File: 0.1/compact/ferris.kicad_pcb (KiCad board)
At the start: 2 copper layers, 208.7 x 86.7 mm, 102 parts, among them J1 USB C, K0_0 KEYSW, K0_1 KEYSW, K0_2 KEYSW, K0_3 KEYSW, K0_4 KEYSW, K0_5 KEYSW, K0_6 KEYSW, K0_7 KEYSW, K0_8 KEYSW, K0_9 KEYSW, K1_0 KEYSW, K1_1 KEYSW, K1_2 KEYSW, K1_3 KEYSW, K1_4 KEYSW, K1_5 KEYSW, K1_6 KEYSW, K1_7 KEYSW, K1_8 KEYSW, K1_9 KEYSW, K2_0 KEYSW, K2_1 KEYSW, K2_2 KEYSW, K2_3 KEYSW, K2_4 KEYSW, K2_5 KEYSW, K2_6 KEYSW, K2_7 KEYSW, K2_8 KEYSW, K2_9 KEYSW, K3_3 KEYSW, K3_4 KEYSW, K3_5 KEYSW, K3_6 KEYSW, SW1 SW_PUSH, U1 ATmega32U4-AU, U2 MCP23017_SO, Y1 Crystal

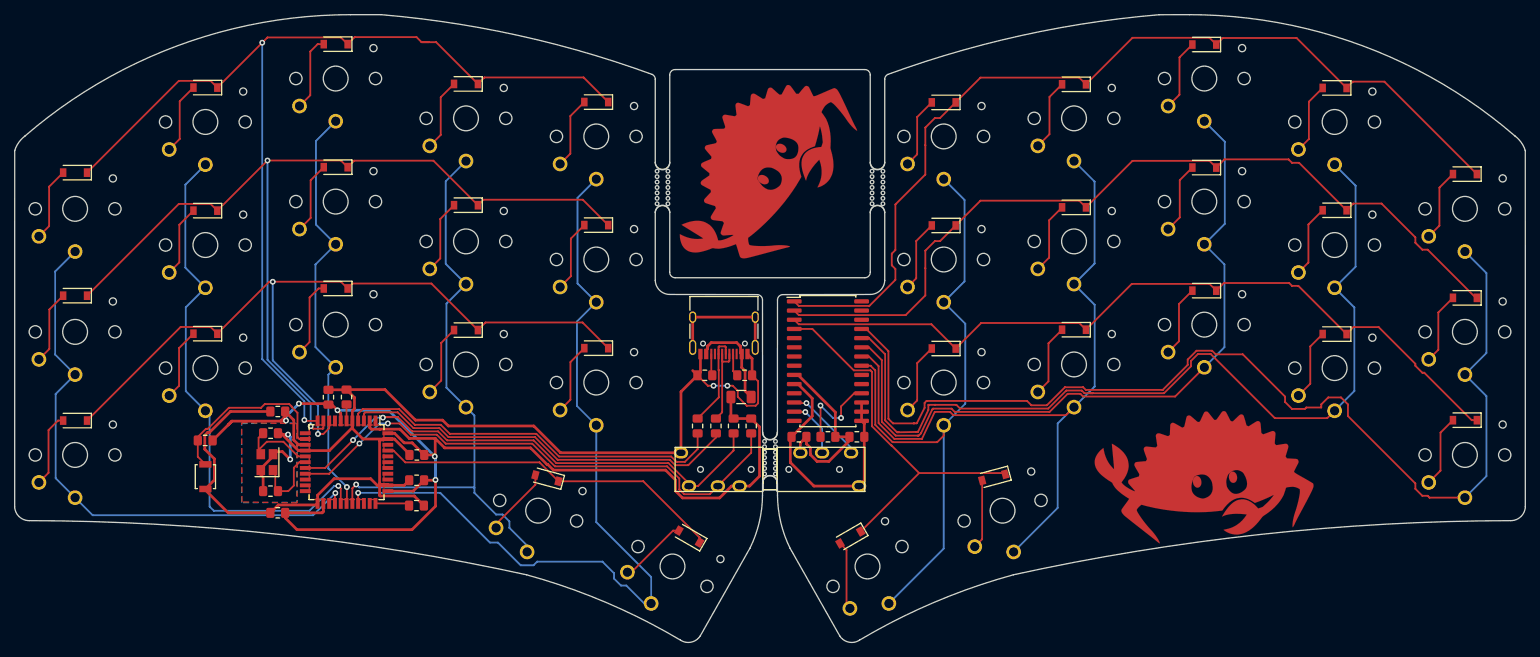
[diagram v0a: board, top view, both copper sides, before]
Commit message: Update to KiCad 7.0
... and prune outdated project files (need to check)
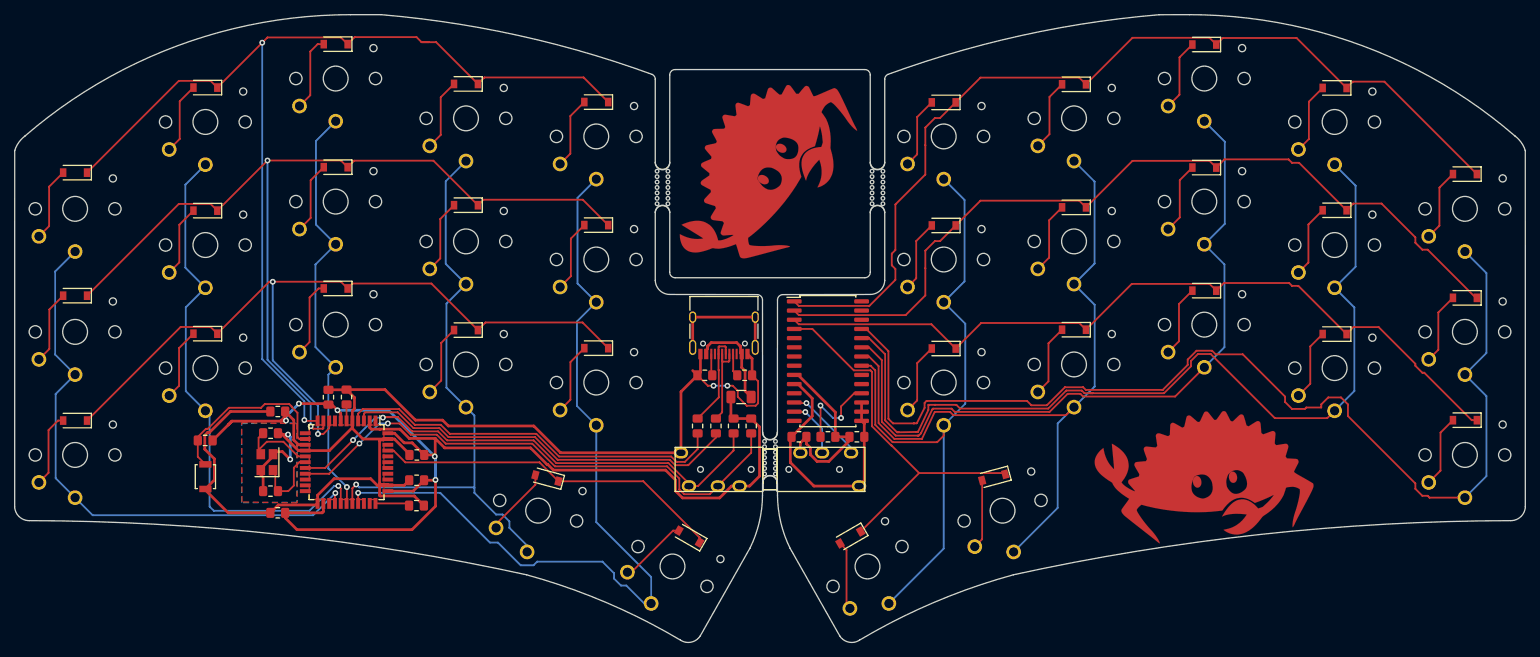
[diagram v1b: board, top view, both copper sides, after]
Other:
- net class Default removed
- net class Power removed
